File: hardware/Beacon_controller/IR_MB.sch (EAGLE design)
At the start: 8 parts, among them U1 ATTINY84ATTINY84-20MU

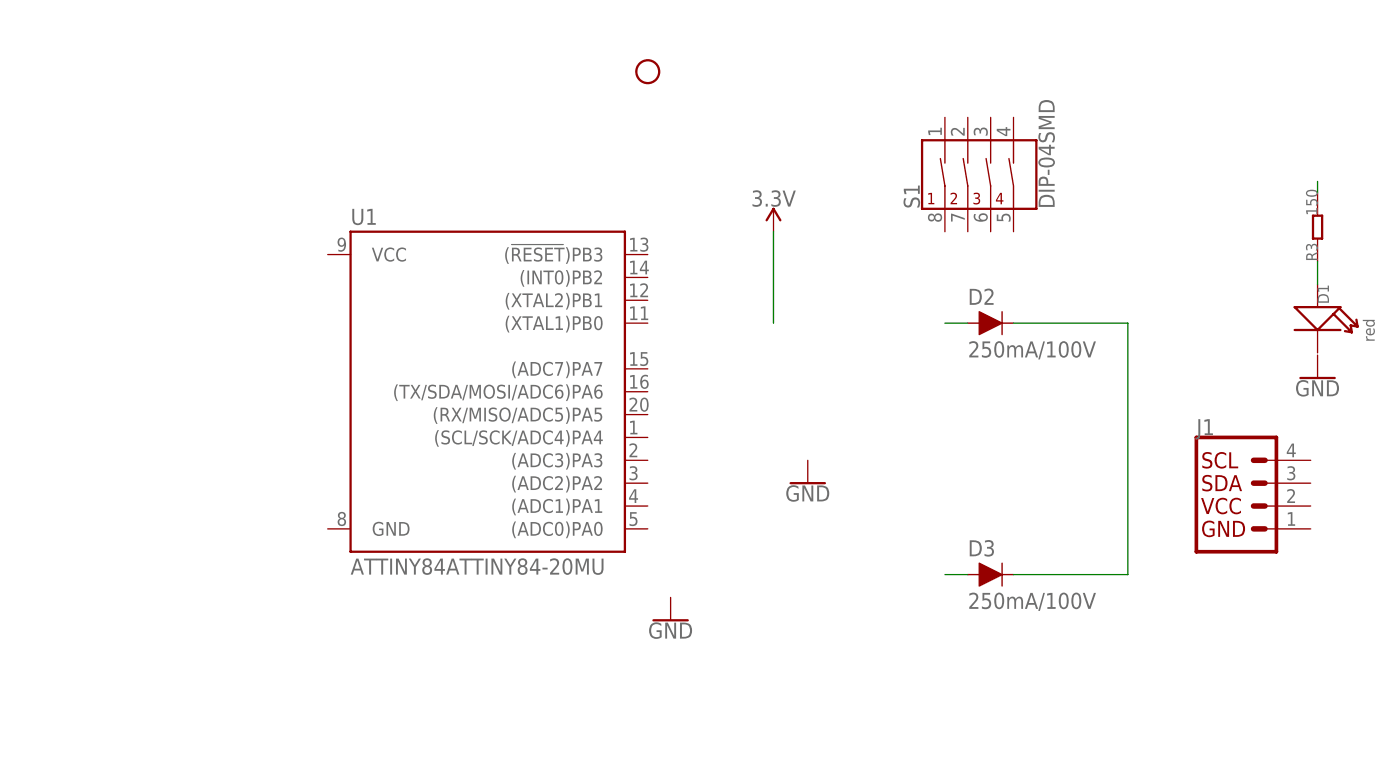
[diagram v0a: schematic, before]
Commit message: Finished Cad files for beacon, and added new 5 bit patern for markers.
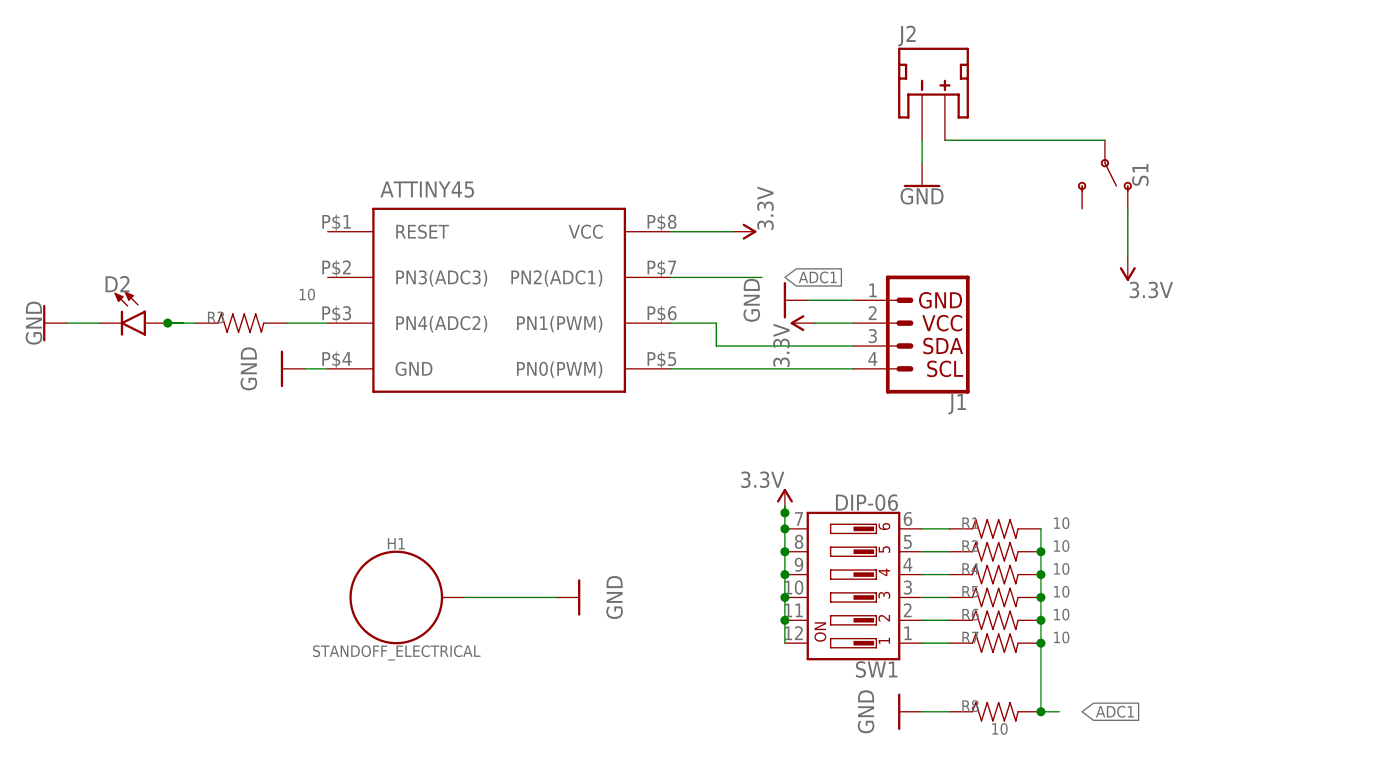
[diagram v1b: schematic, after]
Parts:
- removed D1: red, Discrete:007-LED35*40
- removed D3: 250mA/100V, SparkFun-DiscreteSemi:DIODE-BAS16J
- removed GND: STAND-OFF, SparkFun-Hardware:STAND-OFF
- removed U1: ATTINY84ATTINY84-20MU, SparkFun-IC-Microcontroller:ATTINY84ATTINY84-20MU
- added H1: STANDOFF_ELECTRICAL, IAD-Library:STANDOFF_ELECTRICAL
- added J2: (no value), SparkFun-Connectors:JST_2MM_MALE
- added R1, R2, R4, R5, R6, R7, R8: 10, SparkFun-Resistors:10OHM-1206-1/4W-1%
- added SW1: DIP-06, SparkFun-Switches:DIP-06
- added U$1: ATTINY45, IAD-Library:ATTINY45
- D2: value 250mA/100V -> (none); device SparkFun-DiscreteSemi:DIODE-BAS16J -> SparkFun-LED:LED-FKIT-1206
- R3: value 150 -> 10; device Discrete:005-R0603_S -> SparkFun-Resistors:10OHM-1206-1/4W-1%
- S1: value DIP-04SMD -> (none); device SparkFun-Switches:DIP-04SMD -> SparkFun-Switches:SWITCH-SPDT-PTH-11.6X4.0MM-KIT
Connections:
- new net 3.3V: J1.2, S1.O, SW1.10, SW1.11, SW1.12, SW1.7, SW1.8, SW1.9, U$1.VCC
- new net ADC1: R1.2, R2.2, R4.2, R5.2, R6.2, R7.2, R8.2, U$1.PN2(ADC1)
- new net GND: D2.C, H1.P$1, J1.1, J2.-, R8.1, U$1.GND
- new net N$10: R6.1, SW1.2
- new net N$11: R7.1, SW1.1
- new net N$3: J1.4, U$1.PN0(PWM)
- new net N$4: J1.3, U$1.PN1(PWM)
- new net N$5: J2.+, S1.P
- new net N$8: R4.1, SW1.4
- net N$1: now also U$1.PN4(ADC2)
- net N$2: now also D2.A; no longer D1.+
- net N$6: now also R1.1, SW1.6; no longer D2.A
- net N$7: now also R2.1, SW1.5; no longer D3.A
- net N$9: now also R5.1, SW1.3; no longer D2.C, D3.C
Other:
- moved on the sheet: J1
